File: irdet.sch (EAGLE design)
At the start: 66 parts, among them IC1 MEGA8-AI, IC2 78L05F, J1 PSH02-04WG, J2 PSH02-04WG, J3 PSH02-04WG, J4 PSH02-04WG, J5 22-05-7098-09, T1 S9013, T2 S9012, T3 S9013, T4 S9012, T5 S9013, T6 S9012, T7 S9013, T8 S9012, X1 ARK500/2, X2 ARK500/2

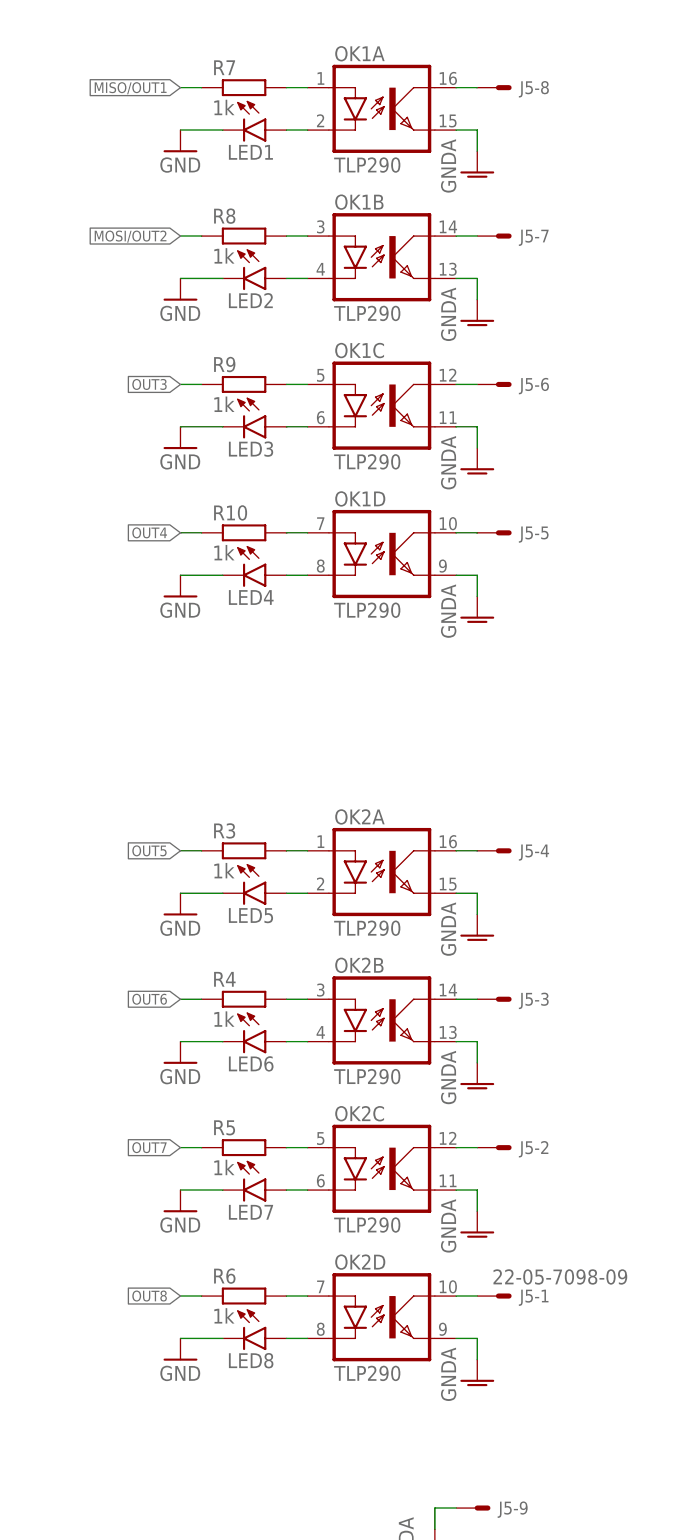
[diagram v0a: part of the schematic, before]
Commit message: TLP290 → TLP292.
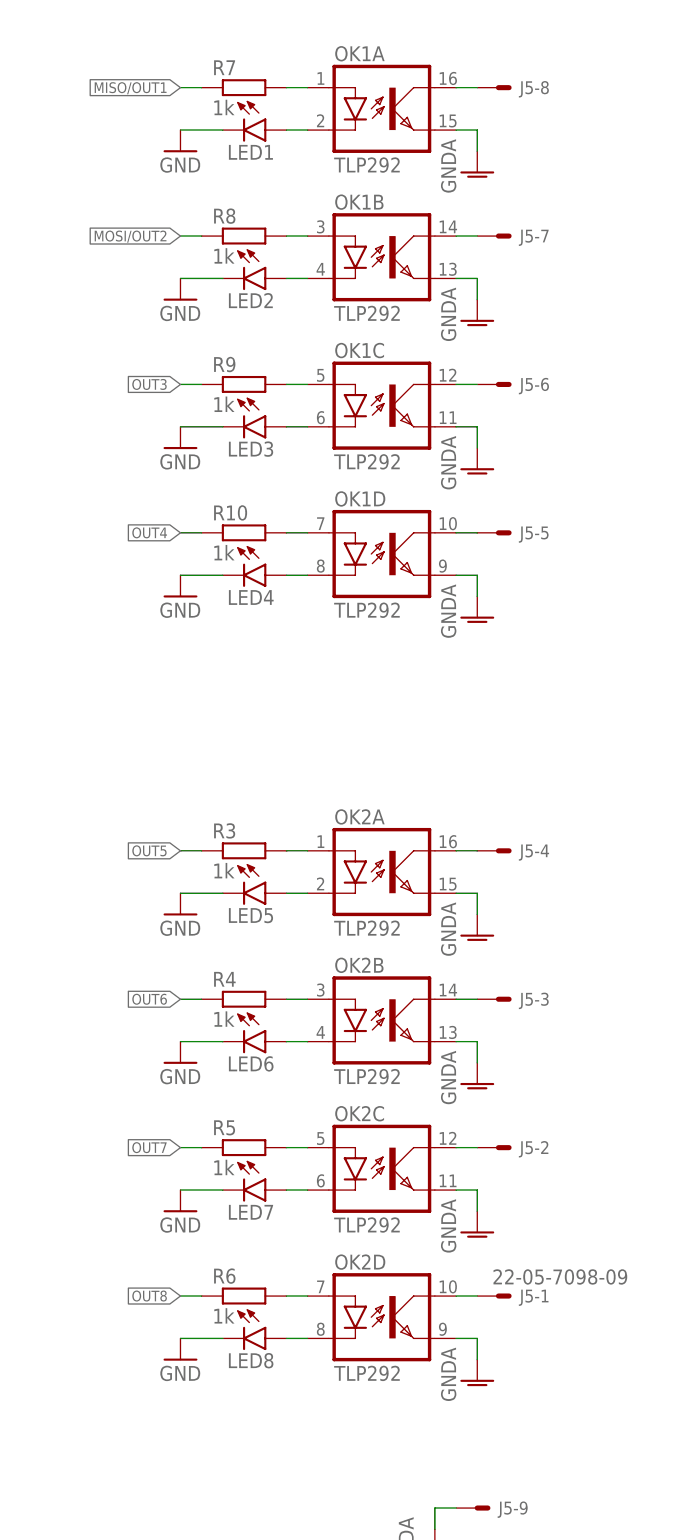
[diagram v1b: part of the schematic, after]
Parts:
- OK1, OK2: value TLP290 -> TLP292
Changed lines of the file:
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@@
 <part name="GND10" library="supply1" library_urn="urn:adsk.eagle:library:371" deviceset="GND" device=""/>
 <part name="D3" library="diode" library_urn="urn:adsk.eagle:library:210" deviceset="CGRM400*-G" device="" package3d_urn="urn:adsk.eagle:package:43457/2" technology="7" value="SM4007PL"/>
-<part name="OK2" library="optocoupler" library_urn="urn:adsk.eagle:library:320" deviceset="TLP283-4" device="" package3d_urn="urn:adsk.eagle:package:21967/1" value="TLP290"/>
+<part name="OK2" library="optocoupler" library_urn="urn:adsk.eagle:library:320" deviceset="TLP283-4" device="" package3d_urn="urn:adsk.eagle:package:21967/1" value="TLP292"/>
 <part name="FRAME1" library="frames" library_urn="urn:adsk.eagle:library:229" deviceset="A3L-LOC" device=""/>
 <part name="R7" library="rcl" deviceset="R-EU_" device="R0805" value="1k"/>
@@
 <part name="GND15" library="supply1" library_urn="urn:adsk.eagle:library:371" deviceset="GND" device=""/>
 <part name="GND16" library="supply1" library_urn="urn:adsk.eagle:library:371" deviceset="GND" device=""/>
-<part name="OK1" library="optocoupler" library_urn="urn:adsk.eagle:library:320" deviceset="TLP283-4" device="" package3d_urn="urn:adsk.eagle:package:21967/1" value="TLP290"/>
+<part name="OK1" library="optocoupler" library_urn="urn:adsk.eagle:library:320" deviceset="TLP283-4" device="" package3d_urn="urn:adsk.eagle:package:21967/1" value="TLP292"/>
 <part name="J5" library="con-molex" library_urn="urn:adsk.eagle:library:165" deviceset="22-?-09" device="05-7098" package3d_urn="urn:adsk.eagle:package:8078658/1"/>
 <part name="GND17" library="supply1" library_urn="urn:adsk.eagle:library:371" deviceset="GNDA" device=""/>

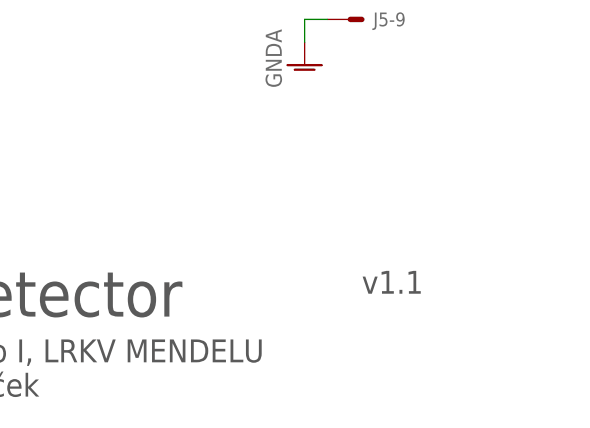
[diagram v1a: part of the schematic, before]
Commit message: Use proper connectors (MVE252-5-V).
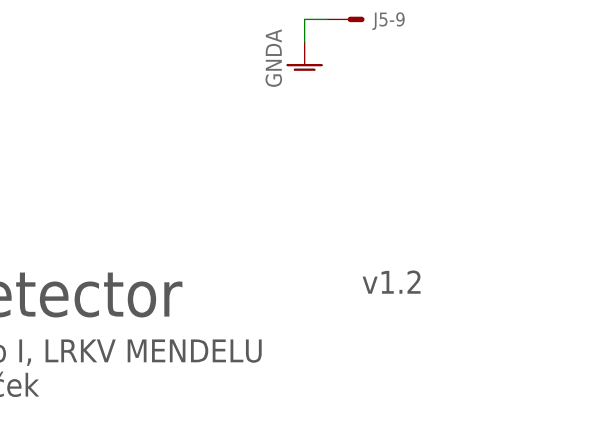
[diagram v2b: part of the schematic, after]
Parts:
- X1, X2: value ARK500/2 -> MVE252-5-V; device con-malina:ARK500/2 -> con-malina:MVE252-5-V
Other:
- note added: "v1.2"
- note removed: "v1.1"
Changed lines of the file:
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@@
 <part name="P+2" library="supply1" library_urn="urn:adsk.eagle:library:371" deviceset="+5V" device="" value="+5V"/>
 <part name="GND2" library="supply1" library_urn="urn:adsk.eagle:library:371" deviceset="GND" device=""/>
-<part name="X1" library="con-malina" deviceset="ARK500/2" device=""/>
+<part name="X1" library="con-malina" deviceset="MVE252-5-V" device=""/>
 <part name="C7" library="rcl" deviceset="C-EU" device="C0805" value="22u"/>
 <part name="C8" library="rcl" deviceset="C-EU" device="C0805" value="22u"/>
@@
 <part name="C16" library="rcl" deviceset="C-EU" device="C0805" value="22u"/>
 <part name="GND30" library="supply1" library_urn="urn:adsk.eagle:library:371" deviceset="GND" device=""/>
-<part name="X2" library="con-malina" deviceset="ARK500/2" device=""/>
+<part name="X2" library="con-malina" deviceset="MVE252-5-V" device=""/>
 </parts>
 <sheets>
@@
 <plain>
 <text x="289.56" y="17.78" size="5.08" layer="97">IR detector</text>
-<text x="344.17" y="20.32" size="2.54" layer="97">v1.1</text>
+<text x="344.17" y="20.32" size="2.54" layer="97">v1.2</text>
 <text x="289.56" y="8.89" size="2.54" layer="97">KMŽ Brno I, LRKV MENDELU
 Jan Horáček</text>

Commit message: Add LCSC numbers to parts.
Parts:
- C1, C10, C11, C12, C13, C14, C15, C2, C4, C5, C6, C9: LCSC_PART (none) -> C49478
- C16, C7, C8: LCSC_PART (none) -> C45783
- D3: LCSC_PART (none) -> C64898
- IC1: LCSC_PART (none) -> C14877
- IC2: LCSC_PART (none) -> C71136
- OK1, OK2: LCSC_PART (none) -> C95713
- R1: LCSC_PART (none) -> C17414
- R10, R3, R4, R5, R6, R7, R8, R9: LCSC_PART (none) -> C17513
- R2: LCSC_PART (none) -> C17520
- RN1, RN2, RN3, RN4: LCSC_PART (none) -> C29718

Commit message: Add CC license.
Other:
- note added: "All"
- note added: "KMŽ Brno I, LRKV MENDELU Jan Horáček 2020-2021"
- note added: "Released under the Creative Commons Attribution-ShareAlike 4.0 License https://creativecommons.org/licenses/by-sa/4.0/ https://github.com/kmzbrnoI/irdet-ele"
- note removed: "KMŽ Brno I, LRKV MENDELU Jan Horáček"
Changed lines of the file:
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@@
 <plain>
 <text x="289.56" y="17.78" size="5.08" layer="97">IR detector</text>
-<text x="344.17" y="20.32" size="2.54" layer="97">v1.2</text>
-<text x="289.56" y="8.89" size="2.54" layer="97">KMŽ Brno I, LRKV MENDELU
-Jan Horáček</text>
+<text x="374.65" y="5.08" size="2.54" layer="94">v1.2</text>
+<text x="289.56" y="5.08" size="2.54" layer="97">KMŽ Brno I, LRKV MENDELU
+Jan Horáček
+2020-2021</text>
+<text x="335.28" y="25.4" size="1.9304" layer="97" align="bottom-center">Released under the Creative Commons Attribution-ShareAlike 4.0 License
+https://creativecommons.org/licenses/by-sa/4.0/
+https://github.com/kmzbrnoI/irdet-ele</text>
+<text x="344.17" y="20.32" size="2.54" layer="94">All</text>
 </plain>
 <instances>

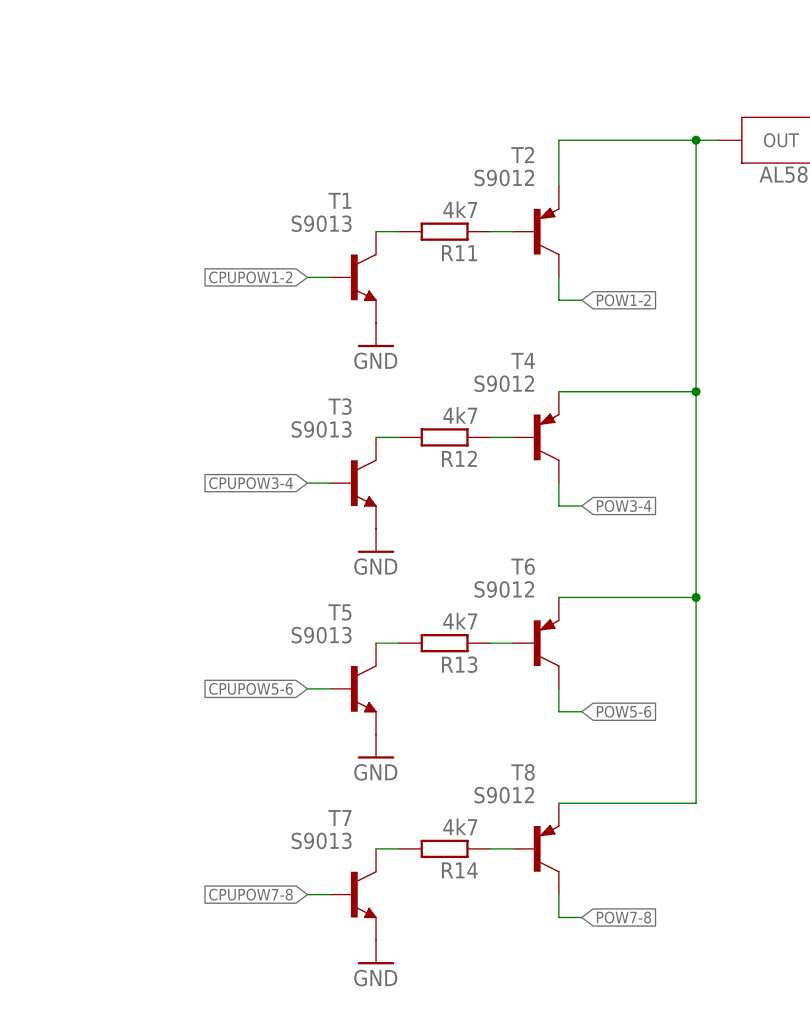
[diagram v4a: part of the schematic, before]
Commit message: Change transistors to more common.
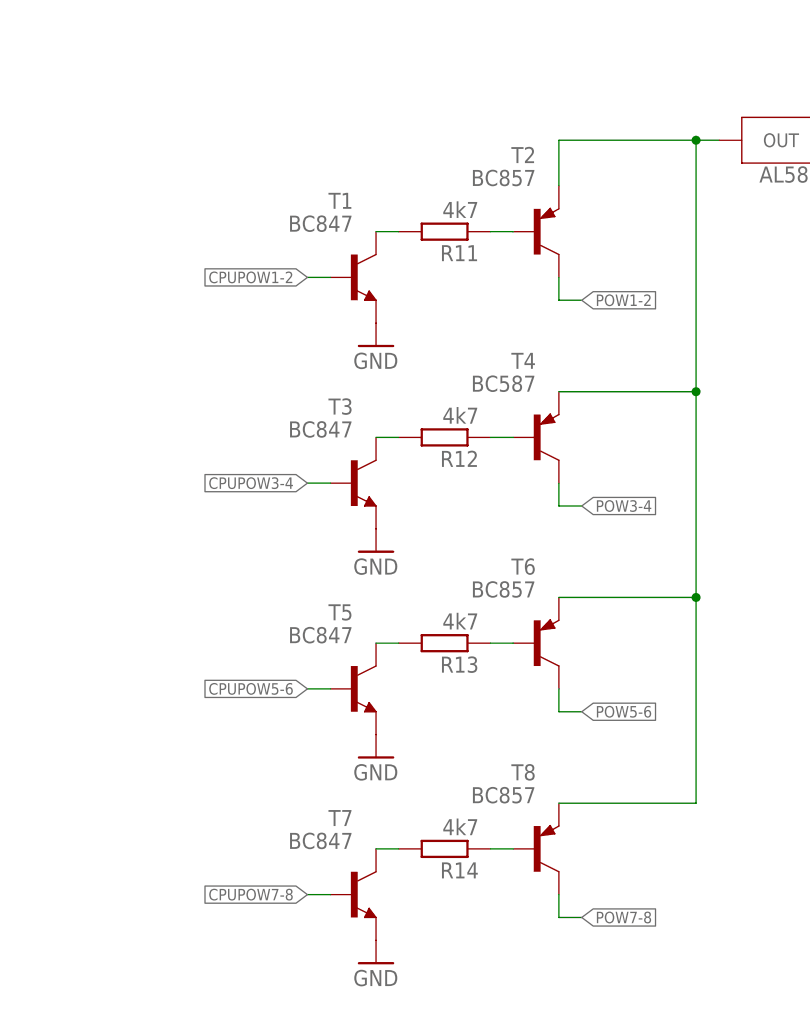
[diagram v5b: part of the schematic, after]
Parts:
- T1, T3, T5, T7: value S9013 -> BC847
- T2, T6, T8: value S9012 -> BC857
- T4: value S9012 -> BC587
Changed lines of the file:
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@@
 <part name="GND24" library="supply1" library_urn="urn:adsk.eagle:library:371" deviceset="GNDA" device=""/>
 <part name="GND25" library="supply1" library_urn="urn:adsk.eagle:library:371" deviceset="GNDA" device=""/>
-<part name="T1" library="transistor" library_urn="urn:adsk.eagle:library:402" deviceset="*-NPN-" device="SOT23-BEC" package3d_urn="urn:adsk.eagle:package:28748/2" technology="BC808" value="S9013"/>
-<part name="T2" library="transistor" library_urn="urn:adsk.eagle:library:402" deviceset="*-PNP-" device="SOT23-BEC" package3d_urn="urn:adsk.eagle:package:28748/2" technology="BC807-16" value="S9012"/>
+<part name="T1" library="transistor" library_urn="urn:adsk.eagle:library:402" deviceset="*-NPN-" device="SOT23-BEC" package3d_urn="urn:adsk.eagle:package:28748/2" technology="BC808" value="BC847"/>
+<part name="T2" library="transistor" library_urn="urn:adsk.eagle:library:402" deviceset="*-PNP-" device="SOT23-BEC" package3d_urn="urn:adsk.eagle:package:28748/2" technology="BC807-16" value="BC857"/>
 <part name="R11" library="rcl" deviceset="R-EU_" device="R0805" value="4k7"/>
 <part name="GND26" library="supply1" library_urn="urn:adsk.eagle:library:371" deviceset="GND" device=""/>
 <part name="P+9" library="supply1" library_urn="urn:adsk.eagle:library:371" deviceset="+12V" device=""/>
 <part name="S1" library="current-stabilizers" deviceset="AL5809" device="" value="AL5809-100"/>
-<part name="T3" library="transistor" library_urn="urn:adsk.eagle:library:402" deviceset="*-NPN-" device="SOT23-BEC" package3d_urn="urn:adsk.eagle:package:28748/2" technology="BC808" value="S9013"/>
-<part name="T4" library="transistor" library_urn="urn:adsk.eagle:library:402" deviceset="*-PNP-" device="SOT23-BEC" package3d_urn="urn:adsk.eagle:package:28748/2" technology="BC807-16" value="S9012"/>
+<part name="T3" library="transistor" library_urn="urn:adsk.eagle:library:402" deviceset="*-NPN-" device="SOT23-BEC" package3d_urn="urn:adsk.eagle:package:28748/2" technology="BC808" value="BC847"/>
+<part name="T4" library="transistor" library_urn="urn:adsk.eagle:library:402" deviceset="*-PNP-" device="SOT23-BEC" package3d_urn="urn:adsk.eagle:package:28748/2" technology="BC807-16" value="BC587"/>
 <part name="R12" library="rcl" deviceset="R-EU_" device="R0805" value="4k7"/>
 <part name="GND27" library="supply1" library_urn="urn:adsk.eagle:library:371" deviceset="GND" device=""/>
-<part name="T5" library="transistor" library_urn="urn:adsk.eagle:library:402" deviceset="*-NPN-" device="SOT23-BEC" package3d_urn="urn:adsk.eagle:package:28748/2" technology="BC808" value="S9013"/>
-<part name="T6" library="transistor" library_urn="urn:adsk.eagle:library:402" deviceset="*-PNP-" device="SOT23-BEC" package3d_urn="urn:adsk.eagle:package:28748/2" technology="BC807-16" value="S9012"/>
+<part name="T5" library="transistor" library_urn="urn:adsk.eagle:library:402" deviceset="*-NPN-" device="SOT23-BEC" package3d_urn="urn:adsk.eagle:package:28748/2" technology="BC808" value="BC847"/>
+<part name="T6" library="transistor" library_urn="urn:adsk.eagle:library:402" deviceset="*-PNP-" device="SOT23-BEC" package3d_urn="urn:adsk.eagle:package:28748/2" technology="BC807-16" value="BC857"/>
 <part name="R13" library="rcl" deviceset="R-EU_" device="R0805" value="4k7"/>
 <part name="GND28" library="supply1" library_urn="urn:adsk.eagle:library:371" deviceset="GND" device=""/>
-<part name="T7" library="transistor" library_urn="urn:adsk.eagle:library:402" deviceset="*-NPN-" device="SOT23-BEC" package3d_urn="urn:adsk.eagle:package:28748/2" technology="BC808" value="S9013"/>
-<part name="T8" library="transistor" library_urn="urn:adsk.eagle:library:402" deviceset="*-PNP-" device="SOT23-BEC" package3d_urn="urn:adsk.eagle:package:28748/2" technology="BC807-16" value="S9012"/>
+<part name="T7" library="transistor" library_urn="urn:adsk.eagle:library:402" deviceset="*-NPN-" device="SOT23-BEC" package3d_urn="urn:adsk.eagle:package:28748/2" technology="BC808" value="BC847"/>
+<part name="T8" library="transistor" library_urn="urn:adsk.eagle:library:402" deviceset="*-PNP-" device="SOT23-BEC" package3d_urn="urn:adsk.eagle:package:28748/2" technology="BC807-16" value="BC857"/>
 <part name="R14" library="rcl" deviceset="R-EU_" device="R0805" value="4k7"/>
 <part name="GND29" library="supply1" library_urn="urn:adsk.eagle:library:371" deviceset="GND" device=""/>

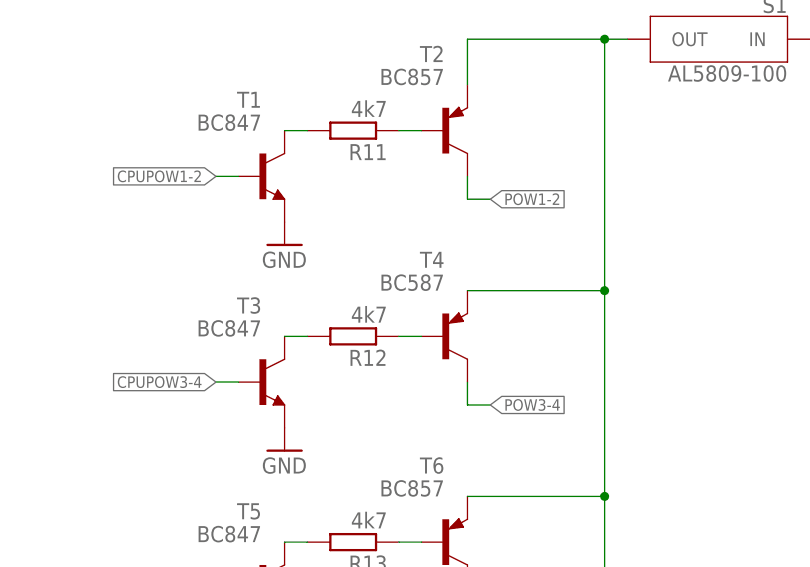
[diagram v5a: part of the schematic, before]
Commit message: Fix bad part value.
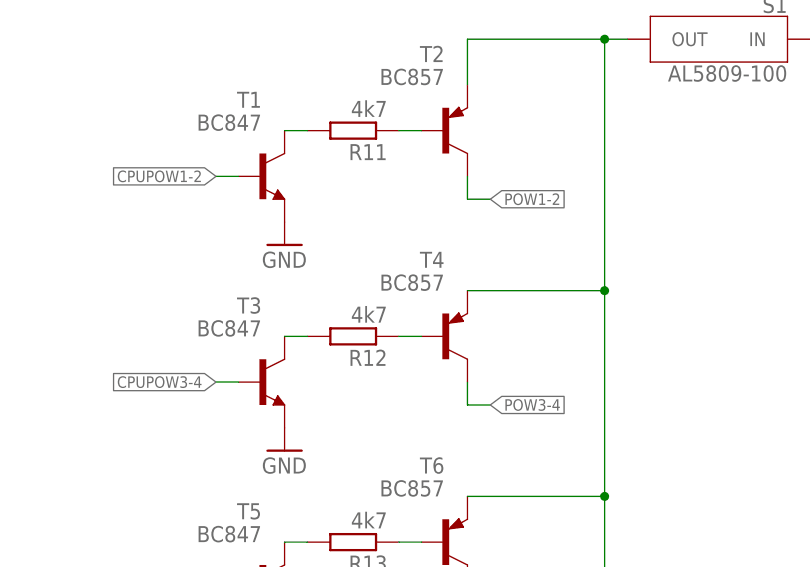
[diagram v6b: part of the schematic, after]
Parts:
- T4: value BC587 -> BC857
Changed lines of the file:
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@@
 <part name="S1" library="current-stabilizers" deviceset="AL5809" device="" value="AL5809-100"/>
 <part name="T3" library="transistor" library_urn="urn:adsk.eagle:library:402" deviceset="*-NPN-" device="SOT23-BEC" package3d_urn="urn:adsk.eagle:package:28748/2" technology="BC808" value="BC847"/>
-<part name="T4" library="transistor" library_urn="urn:adsk.eagle:library:402" deviceset="*-PNP-" device="SOT23-BEC" package3d_urn="urn:adsk.eagle:package:28748/2" technology="BC807-16" value="BC587"/>
+<part name="T4" library="transistor" library_urn="urn:adsk.eagle:library:402" deviceset="*-PNP-" device="SOT23-BEC" package3d_urn="urn:adsk.eagle:package:28748/2" technology="BC807-16" value="BC857"/>
 <part name="R12" library="rcl" deviceset="R-EU_" device="R0805" value="4k7"/>
 <part name="GND27" library="supply1" library_urn="urn:adsk.eagle:library:371" deviceset="GND" device=""/>

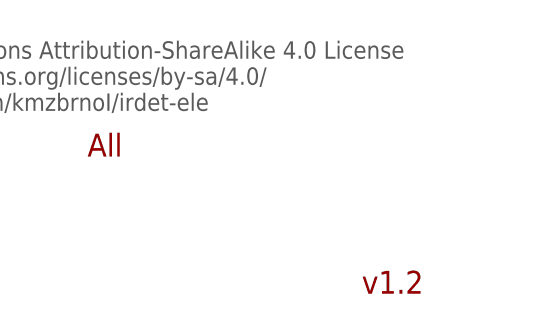
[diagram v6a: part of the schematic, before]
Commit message: Fix shortcut on PCB.
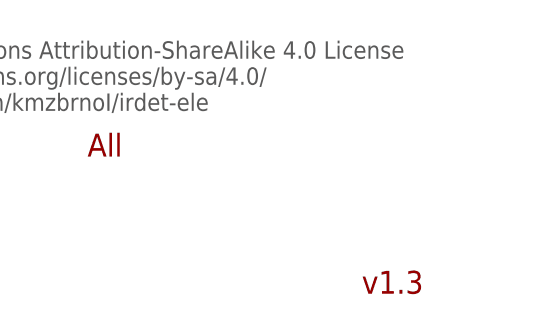
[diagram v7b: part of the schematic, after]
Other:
- note added: "v1.3"
- note removed: "v1.2"
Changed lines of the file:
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@@
 <plain>
 <text x="289.56" y="17.78" size="5.08" layer="97">IR detector</text>
-<text x="374.65" y="5.08" size="2.54" layer="94">v1.2</text>
+<text x="374.65" y="5.08" size="2.54" layer="94">v1.3</text>
 <text x="289.56" y="5.08" size="2.54" layer="97">KMŽ Brno I, LRKV MENDELU
 Jan Horáček
